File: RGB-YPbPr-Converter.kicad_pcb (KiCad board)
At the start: 2 copper layers, 54.5 x 35 mm, 33 parts, among them J1 RGB, J2 Component, J3 PWR, U1 LMV7219M5, U2 LT6550, U3 ICL7660

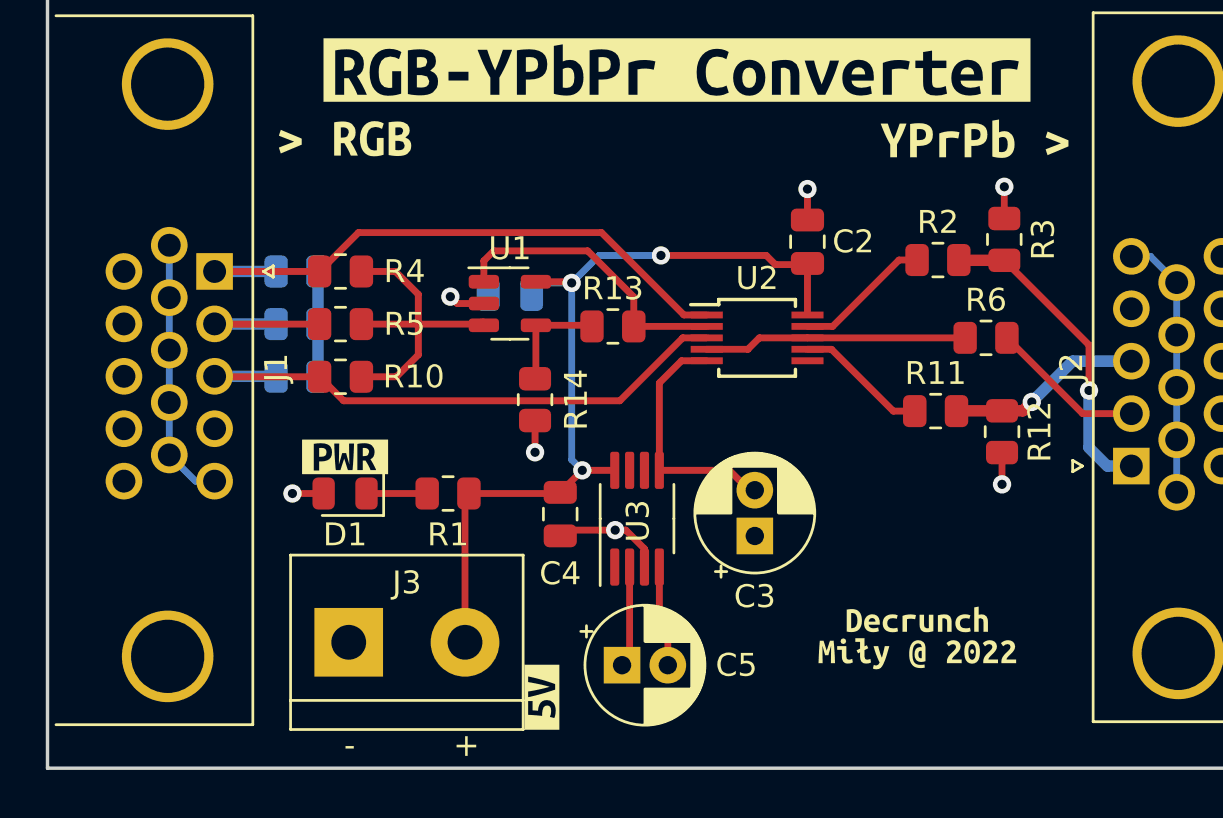
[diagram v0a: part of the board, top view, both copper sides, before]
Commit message: Add H and V sync pulses to Y channel
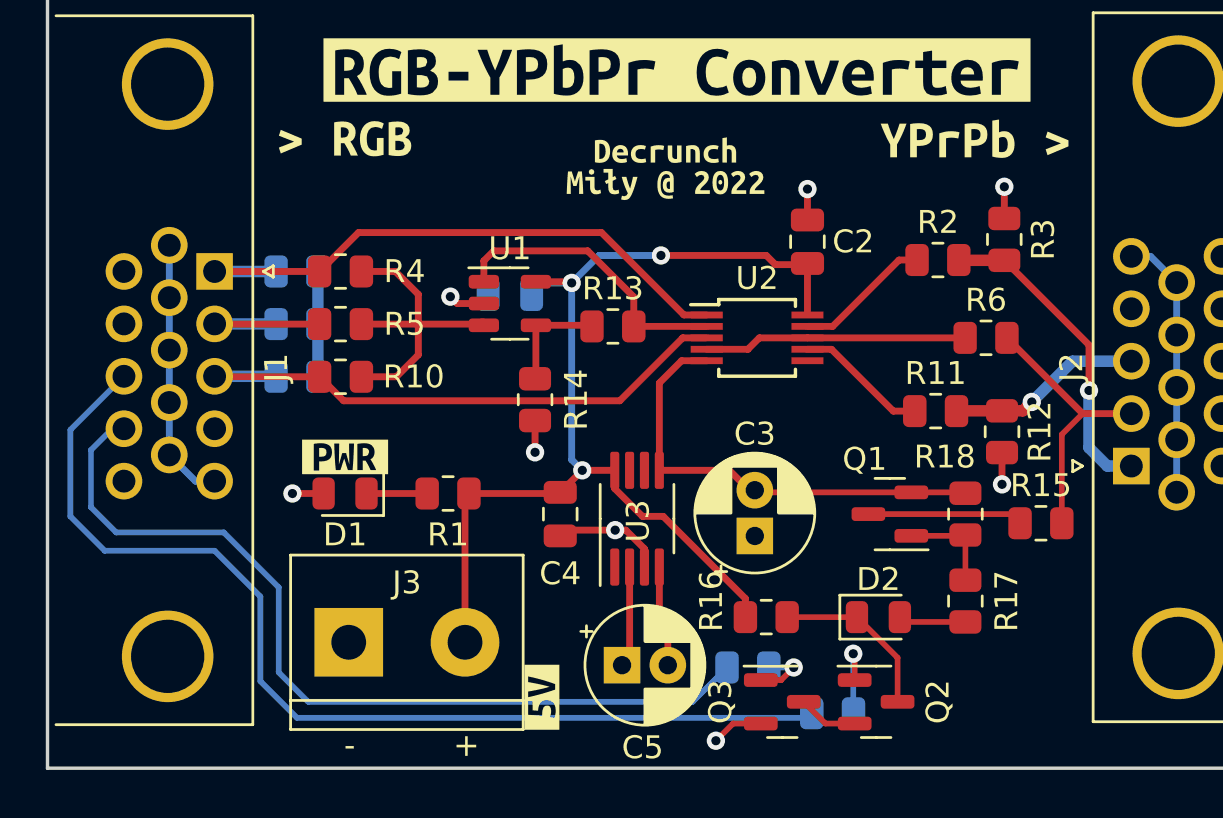
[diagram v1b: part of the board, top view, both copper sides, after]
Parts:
- added D2: 5.6V, Diode_SMD:D_0805_2012Metric, F.Cu at (97.8, 81.9)
- added Q1: Q_NPN_BEC, Package_TO_SOT_SMD:SOT-23, F.Cu at (98.3, 77.4)
- added Q2: Q_NPN_BEC, Package_TO_SOT_SMD:SOT-23, F.Cu at (97.7, 85.6)
- added Q3: Q_NPN_BEC, Package_TO_SOT_SMD:SOT-23, F.Cu at (93.6, 85.6)
- added R15: 570, Resistor_SMD:R_0805_2012Metric, F.Cu at (104.9, 77.8)
- added R16: 1k, Resistor_SMD:R_0805_2012Metric, F.Cu at (92.9, 81.9)
- added R17: 1k, Resistor_SMD:R_0805_2012Metric, F.Cu at (101.6, 81.2)
- added R18: 1k, Resistor_SMD:R_0805_2012Metric, F.Cu at (101.6, 77.4)
- added R19: 1k, Resistor_SMD:R_0805_2012Metric, B.Cu at (95.8, 86.1)
- added R20: 1k, Resistor_SMD:R_0805_2012Metric, B.Cu at (92.1, 84.1)
- U1: value LMV7219M5 -> LMV793MFX
- moved kibuzzard-63377C0B 23.3 mm to (88.5, 63.0)
- moved kibuzzard-63377C27 23.3 mm to (88.5, 61.5)
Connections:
- J1 pad 13: unconnected-(J1-Pad13) -> /H_SYNC
- J1 pad 14: unconnected-(J1-Pad14) -> /V_SYNC
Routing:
- net /H_SYNC: track 0.00 -> 45.4 mm
- net /V_SYNC: track 0.00 -> 38.4 mm
- net +5V: track 38.4 -> 47.7 mm
- net -5V: track 10.8 -> 20.1 mm
- net Net-(D2-Pad1): track 0.00 -> 7.49 mm
- net Net-(Q1-Pad3): track 0.00 -> 6.79 mm
- net /Y: track 6.81 -> 12.0 mm
- net Net-(Q1-Pad1): track 0.00 -> 4.35 mm
- net Net-(Q2-Pad1): track 0.00 -> 3.78 mm, vias 0 -> 1
- net Net-(D2-Pad2): track 0.00 -> 2.95 mm
- net Net-(Q3-Pad1): track 0.00 -> 2.75 mm, vias 0 -> 1
- net Net-(Q2-Pad2): track 0.00 -> 2.62 mm
- net GND: track 41.2 -> 43.5 mm, vias 7 -> 8

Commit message: finished board
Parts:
- removed the J2 at (108.8, 75.3)
- removed kibuzzard-63377BCB: G***, kibuzzard-63377BCB
- removed kibuzzard-63377BDE: G***, kibuzzard-63377BDE
- removed kibuzzard-63377C0B: G***, kibuzzard-63377C0B
- removed kibuzzard-63377C27: G***, kibuzzard-63377C27
- removed kibuzzard-63377CAE: G***, kibuzzard-63377CAE
- removed kibuzzard-63377D38: G***, kibuzzard-63377D38
- added C1: 10u/16V, Capacitor_THT:CP_Radial_D5.0mm_P2.00mm, F.Cu at (123.1, 163.5)
- added C2: 100n, Capacitor_SMD:C_0805_2012Metric, F.Cu at (129.5, 156.1)
- added C3: 100n, Capacitor_SMD:C_0805_2012Metric, F.Cu at (133.3, 156.1)
- added C9: 100n, Capacitor_SMD:C_0805_2012Metric, F.Cu at (138.2, 131.4)
- added D1: 1N4001, Diode_THT:D_DO-41_SOD81_P10.16mm_Horizontal, F.Cu at (118.2, 162.0)
- added H1: DNP, MountingHole:MountingHole_3.2mm_M3_ISO7380_Pad, F.Cu at (104.0, 104.0)
- added H2: DNP, MountingHole:MountingHole_3.2mm_M3_ISO7380_Pad, F.Cu at (166.0, 104.0)
- added H3: DNP, MountingHole:MountingHole_3.2mm_M3_ISO7380_Pad, F.Cu at (104.0, 166.0)
- added H4: DNP, MountingHole:MountingHole_3.2mm_M3_ISO7380_Pad, F.Cu at (166.0, 166.0)
- added J1: Barrel Jack 5.5/2.1, Connector_BarrelJack:BarrelJack_Horizontal, F.Cu at (113.8, 151.9)
- added J4: BNC 75 Ohm, Connector_Coaxial:BNC_Amphenol_B6252HB-NPP3G-50_Horizontal, F.Cu at (156.4, 135.0)
- added J5: BNC 75 Ohm, Connector_Coaxial:BNC_Amphenol_B6252HB-NPP3G-50_Horizontal, F.Cu at (156.4, 154.1)
- added R1: 75, Resistor_SMD:R_0805_2012Metric, F.Cu at (122.0, 146.8)
- added R15: 0R, Resistor_SMD:R_0805_2012Metric, F.Cu at (127.7, 134.7)
- added R2: 75, Resistor_SMD:R_0805_2012Metric, F.Cu at (122.0, 139.8)
- added U1: 1117-5.0, Package_TO_SOT_SMD:SOT-223, F.Cu at (131.4, 161.8)
- added kibuzzard-633F44A8: G***, kibuzzard-633F44A8, F.Cu at (151.9, 152.8)
- added kibuzzard-633F44BA: G***, kibuzzard-633F44BA, F.Cu at (151.8, 114.6)
- added kibuzzard-633F44C9: G***, kibuzzard-633F44C9, F.Cu at (151.9, 133.7)
- added kibuzzard-633F4DF1: G***, kibuzzard-633F4DF1, F.Cu at (104.1, 158.3)
- C5: renamed from C1; moved to F.Cu
- C6: renamed from C5; value 10u -> 10u/16V
- C7: renamed from C3; value 10u -> 10u/16V
- D2: footprint Diode_SMD:D_0805_2012Metric -> Diode_SMD:D_SOD-323_HandSoldering
- J2: renamed from J1; value RGB -> D-Sub HD15 Female; footprint Connector_Dsub:DSUB-15-HD_Male_Horizontal_P2.29x1.98mm_EdgePinOffset3.03mm_Housed_MountingHolesOffset4.94mm -> lib:ICD15S13E4GV00LF
- J3: value PWR -> BNC 75 Ohm; footprint TerminalBlock:TerminalBlock_bornier-2_P5.08mm -> Connector_Coaxial:BNC_Amphenol_B6252HB-NPP3G-50_Horizontal
- R3: renamed from R20; moved to F.Cu
- R4: renamed from R19; moved to F.Cu
- R5: renamed from R7; moved to F.Cu
- R6: renamed from R8; moved to F.Cu
- R7: renamed from R9; moved to F.Cu
- U2: renamed from U3; footprint Package_SO:MSOP-8_3x3mm_P0.65mm -> Package_SO:SOIC-8_3.9x4.9mm_P1.27mm
- moved C7 100.1 mm to (145.0, 163.5), turned to 0 degrees
- moved U2 97.6 mm to (142.9, 157.7), turned to 0 degrees
- moved C4 96.5 mm to (143.0, 153.7), turned to 180 degrees
- moved C6 95.4 mm to (139.3, 163.5)
- moved D3 92.5 mm to (110.1, 161.9), turned to 0 degrees
- moved R18 92.3 mm to (113.9, 161.9), turned to 0 degrees
- moved J3 88.1 mm to (156.4, 116.0), turned to -90 degrees
- moved R9 81.4 mm to (121.9, 132.8)
- moved R7 80.9 mm to (121.9, 130.8)
- moved R23 78.6 mm to (144.7, 132.2), turned to 180 degrees
- moved C5 78.4 mm to (126.8, 131.9)
- moved R10 76.3 mm to (121.9, 128.8)
- moved R6 76.0 mm to (121.9, 126.8)
- moved R8 75.7 mm to (127.4, 149.3), turned to 90 degrees
- moved Q3 75.5 mm to (140.5, 140.0), turned to 0 degrees
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- renumbered C2 to C8, D1 to D3, Q2 to Q1, Q3 to Q2, Q1 to Q3, R5 to R10, R10 to R11, R17 to R12, R14 to R13, R18 to R14, R13 to R16, R15 to R17, R1 to R18, R2 to R19, R11 to R20, R12 to R21, R6 to R22, R3 to R23, R16 to R8, R4 to R9, U1 to U3, U2 to U4
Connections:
- net /Y_FB renamed /Y_OUT
- net Net-(C5-Pad1) renamed /CAP+
- net Net-(C5-Pad2) renamed /CAP-
- net Net-(R10-Pad2) renamed /YSUM
- net Net-(R11-Pad1) renamed /Pr_OUT
- net Net-(R13-Pad1) renamed /FB
- net Net-(R13-Pad2) renamed /YAMP
- net Net-(R2-Pad1) renamed /Pb_OUT
- C5 pad 1: +5V -> /+5VAMP
- D3 pad 1: Net-(D1-Pad1) -> GND
- D3 pad 2: GND -> Net-(D3-Pad2)
- J2 pad 9: GND -> unconnected-(J2-Pad9)
- J3 pad 1: GND -> /Pb
- J3 pad 2: +5V -> GND
- Q1 pad 1: Net-(Q2-Pad1) -> /V_R
- Q2 pad 1: Net-(Q3-Pad1) (its old number) -> /H_R
- R18 pad 1: +5V -> Net-(D3-Pad2)
- R18 pad 2: Net-(D1-Pad1) -> +5V
- R19 pad 2: /Pr -> /Pb
- R20 pad 2: /Pb -> /Pr
- R3 pad 2: Net-(Q3-Pad1) (its old number) -> /V_R
- R4 pad 2: Net-(Q2-Pad1) -> /H_R
- U3 pad 5: +5V -> /+5VAMP
- U4 pad 1: /R -> /B
- U4 pad 3: /B -> /R
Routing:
- net +5V: track 47.7 -> 213.4 mm, vias 3 -> 0
- net -5V: track 20.1 -> 56.1 mm
- net /VIND: track 0.00 -> 19.7 mm
- net /Pr: track 13.9 -> 33.1 mm, vias 1 -> 0
- net /Y: track 12.0 -> 23.7 mm
- net /Pb: track 8.54 -> 19.6 mm, vias 1 -> 0
- net GND: track 43.5 -> 54.1 mm, vias 8 -> 17
- net /H_SYNC: track 45.4 -> 34.9 mm
- net /V_SYNC: track 38.4 -> 45.3 mm
- net Net-(D2-Pad1): track 7.49 -> 14.3 mm
- net /V_R: track 0.00 -> 6.70 mm
- net /H_R: track 0.00 -> 6.49 mm
- net /B: track 25.7 -> 31.6 mm
- net /CAP+: track 4.42 -> 8.94 mm
- net /VIN: track 0.00 -> 4.45 mm
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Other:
- board size 54.5 x 35 mm -> 70 x 70 mm
- board text added: "Transmission line geometry: h = 1.55mm Er = 4.5 (JLCPCB 2-layer) Copper = 35um (1oz) w = 1.3mm Zo = 75 Ohm Calculated using Saturn PCB Toolkit."
- board text added: "blackwine/Miły/Kosmolot Decrunch 2022"
- board text removed: "+"
- board text removed: "-"
- board text removed: "JLCJLCJLC"

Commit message: fixes
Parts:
- added R12: 0R, Resistor_SMD:R_0805_2012Metric, F.Cu at (122.0, 134.2)
- added R13: 0R, Resistor_SMD:R_0805_2012Metric, F.Cu at (122.0, 128.8)
- added R14: 0R, Resistor_SMD:R_0805_2012Metric, F.Cu at (122.0, 123.5)
- added R25: 0R, Resistor_SMD:R_0805_2012Metric, F.Cu at (148.2, 126.2)
- added R26: 0R, Resistor_SMD:R_0805_2012Metric, F.Cu at (148.2, 131.6)
- added R28: 0R, Resistor_SMD:R_0805_2012Metric, F.Cu at (144.7, 124.2)
- added R30: 0R, Resistor_SMD:R_0805_2012Metric, F.Cu at (144.7, 133.6)
- C2, C3, C4, C5, C8, C9: value 100n -> 100n/16V
- D3: value PWR -> Green
- R21: renamed from R19; value 105 -> 133
- R22: value 105 -> 75
- moved kibuzzard-633F44BA 19.1 mm to (151.8, 133.7)
- moved J3 19.0 mm to (156.4, 135.0)
- moved J4 19.0 mm to (156.4, 116.0)
- moved kibuzzard-633F44C9 19.0 mm to (151.9, 114.7)
- moved R22 12.5 mm to (147.2, 116.0)
- moved R29 3.77 mm to (148.2, 133.6)
- moved R9 3.74 mm to (118.5, 134.2)
- moved R11 3.67 mm to (118.5, 123.5)
- moved R10 3.51 mm to (118.4, 128.8)
- moved R27 3.50 mm to (148.2, 124.2)
- moved R20 2.40 mm to (144.7, 138.1)
- moved R7 1.47 mm to (121.9, 132.2)
- moved R23 1.40 mm to (144.7, 131.6)
- moved R3 1.25 mm to (121.9, 121.5)
- renumbered R12 to R15, R13 to R16, R14 to R17, R15 to R18, R16 to R19, R17 to R20, R20 to R23, R18 to R24, R21 to R27, R23 to R29, R5 to R3, R3 to R4, R4 to R5
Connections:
- R10 pad 2: /YSUM -> Net-(R10-Pad2)
- R11 pad 2: /YSUM -> Net-(R11-Pad2)
- R21 pad 2: /Pb -> Net-(R21-Pad2)
- R23 pad 2: /Pr -> Net-(R23-Pad2)
- R27 pad 2: GND -> Net-(R27-Pad2)
- R29 pad 2: GND -> Net-(R29-Pad2)
- R9 pad 2: /YSUM -> Net-(R12-Pad1)
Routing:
- net /Y_OUT: track 7.99 -> 22.2 mm
- net /Y: track 23.7 -> 32.1 mm
- net /Pr: track 33.1 -> 28.9 mm
- net /R: track 30.0 -> 33.9 mm
- net /YSUM: track 13.5 -> 16.3 mm
- net +5V: track 213.4 -> 216.1 mm
- net /Pb: track 19.6 -> 17.1 mm
- net Net-(Q3-Pad3): track 6.12 -> 4.13 mm
- net /Pr_OUT: track 4.01 -> 5.70 mm
- net Net-(R10-Pad2): track 0.00 -> 1.69 mm
- net Net-(R29-Pad2): track 0.00 -> 1.67 mm
- net Net-(R27-Pad2): track 0.00 -> 1.67 mm
- net Net-(R23-Pad2): track 0.00 -> 1.67 mm
- net Net-(R21-Pad2): track 0.00 -> 1.67 mm
- net Net-(R11-Pad2): track 0.00 -> 1.63 mm
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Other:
- board text added: "https://www.analog.com/media/en/technical-documentation/data-sheets/65501fa.pdf https://www.analog.com/media/en/technical-documentation/application-notes/an57fa.pdf"

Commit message: emergency version for decrunch 2023
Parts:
- removed C7: 10u/16V, Capacitor_THT:CP_Radial_D5.0mm_P2.00mm
- removed D1: 1N4001, Diode_THT:D_DO-41_SOD81_P10.16mm_Horizontal
- removed R1, R2: 75, Resistor_SMD:R_0805_2012Metric
- removed R18: 0R, Resistor_SMD:R_0805_2012Metric
- removed U3: LMV793MFX, Package_TO_SOT_SMD:SOT-23-5
- removed kibuzzard-633F4DF1: G***, kibuzzard-633F4DF1
- added U5: AD818ARZ, Package_SO:SO-8_3.9x4.9mm_P1.27mm, F.Cu at (128.9, 127.0)
- C6: value 10u/16V -> 100n/16V; footprint Capacitor_THT:CP_Radial_D5.0mm_P2.00mm -> Capacitor_SMD:C_0805_2012Metric
- R24: value 1k -> 10k
- U2: value ICL7660 -> 1117-5.0; footprint Package_SO:SOIC-8_3.9x4.9mm_P1.27mm -> Package_TO_SOT_SMD:SOT-223
- moved C1 12.3 mm to (118.9, 151.9)
- moved C6 7.73 mm to (137.1, 156.1)
- moved R16 7.16 mm to (127.0, 123.2), turned to 0 degrees
- moved U2 5.76 mm to (138.9, 161.8), turned to -90 degrees
- moved R19 5.57 mm to (130.9, 123.3), turned to 0 degrees
- moved C4 3.28 mm to (140.8, 156.1), turned to 0 degrees
- moved C5 2.30 mm to (128.8, 130.8)
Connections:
- C1 pad 1: /VIND -> /VIN
- C1 pad 2: GND -> -5V
- C2 pad 1: /VIND -> /VIN
- C2 pad 2: GND -> -5V
- C3 pad 1: +5V -> GND
- C3 pad 2: GND -> -5V
- C5 pad 1: /+5VAMP -> +5V
- C5 pad 2: GND -> -5V
- C6 pad 1: /CAP+ -> /VIN
- C6 pad 2: /CAP- -> GND
- D3 pad 1: GND -> -5V
- J1 pad 2: GND -> -5V
- J1 pad 3: GND -> -5V
- R24 pad 2: +5V -> /VIN
- U1 pad 1: GND -> -5V
- U1 pad 2: +5V -> GND
- U1 pad 3: /VIND -> /VIN
- U2 pad 1: unconnected-(U2-Pad1) -> GND
- U2 pad 2: /CAP+ -> +5V
- U2 pad 3: GND -> /VIN
- U2 pad 4: /CAP- -> (no net)
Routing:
- net +5V: track 216.1 -> 64.2 mm, vias 0 -> 6
- net /VIN: track 4.45 -> 55.4 mm
- net -5V: track 55.4 -> 97.3 mm, vias 0 -> 6
- net /VIND: track 19.7 -> 0.00 mm
- net GND: track 54.4 -> 37.9 mm, vias 16 -> 13
- net /CAP+: track 8.94 -> 0.00 mm
- net /CAP-: track 4.23 -> 0.00 mm
- net /+5VAMP: track 3.97 -> 0.00 mm
- net /V_SYNC: track 45.3 -> 43.3 mm
- net /H_SYNC: track 34.9 -> 32.9 mm
- net /R: track 33.9 -> 34.5 mm
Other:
- board text added: "12V"
- board text added: "blackwine/Miły/Kosmolot Decrunch 2023"
- board text removed: "blackwine/Miły/Kosmolot Decrunch 2022"

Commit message: gerbers + resistor values
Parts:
- R10: value 549 -> 510
- R11: value 2940 -> 2700
- R12: value 0R -> 510
- R13, R30: value 0R -> 39
- R14: value 0R -> 220
- R20: value 570 -> 560
- R21: value 133 -> 120
- R23: value 105 -> 100
- R25: value 0R -> 12
- R26: value 0R -> 3.9
- R27: value 174 -> 120
- R28: value 0R -> 51
- R29: value 261 -> 220
- R9: value 1070 -> 560
